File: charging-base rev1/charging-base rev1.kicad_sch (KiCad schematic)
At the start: 11 parts, among them J1 Barrel_Jack, J2 PowerToDino, Q1 NMOS, U1 LM358_DFN

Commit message: added some power questions
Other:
- note added: "What is max current draw of dino? What is current draw of dino when chargning is done? Does current draw change if dino is switched on or switched off? Does the raspi load the source, or is the only load on this circuit the USB battery pack?"
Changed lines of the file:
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@@
+    (effects (font (size 1.27 1.27)) (justify left bottom))
+  )
+  (text "What is max current draw of dino?\nWhat is current draw of dino when chargning is done?\nDoes current draw change if dino is switched on or switched off?\nDoes the raspi load the source, or is the only load on this circuit the USB battery pack?"
+    (at 167.005 127.635 0)
     (effects (font (size 1.27 1.27)) (justify left bottom))
   )

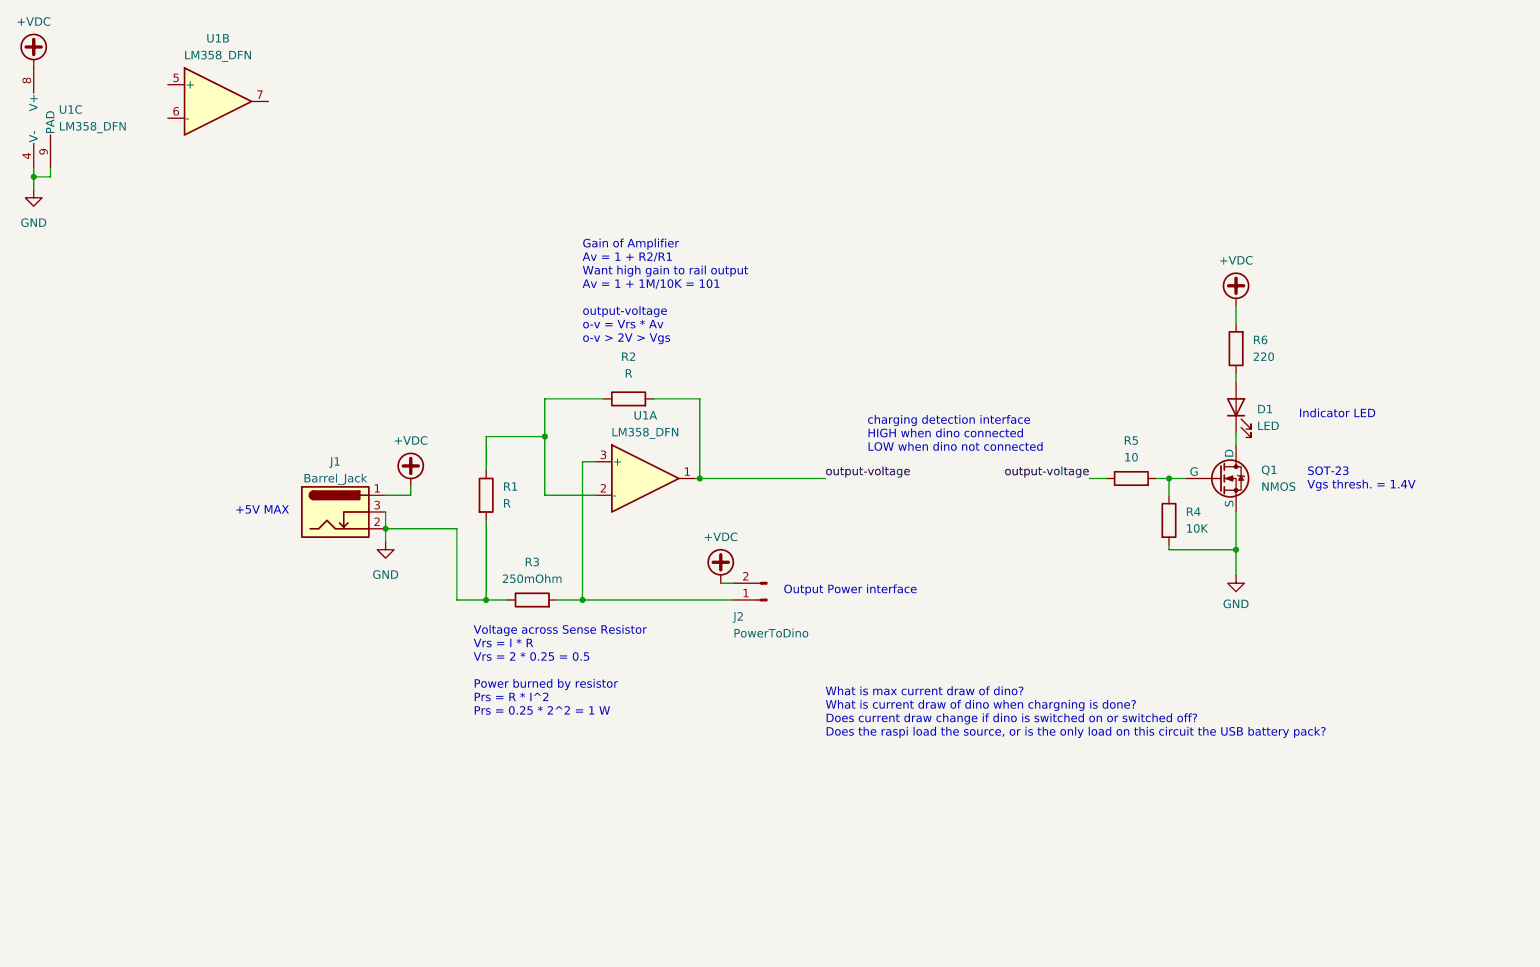
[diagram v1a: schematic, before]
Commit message: finished rev1 of layout, resistor sensor not yet selected
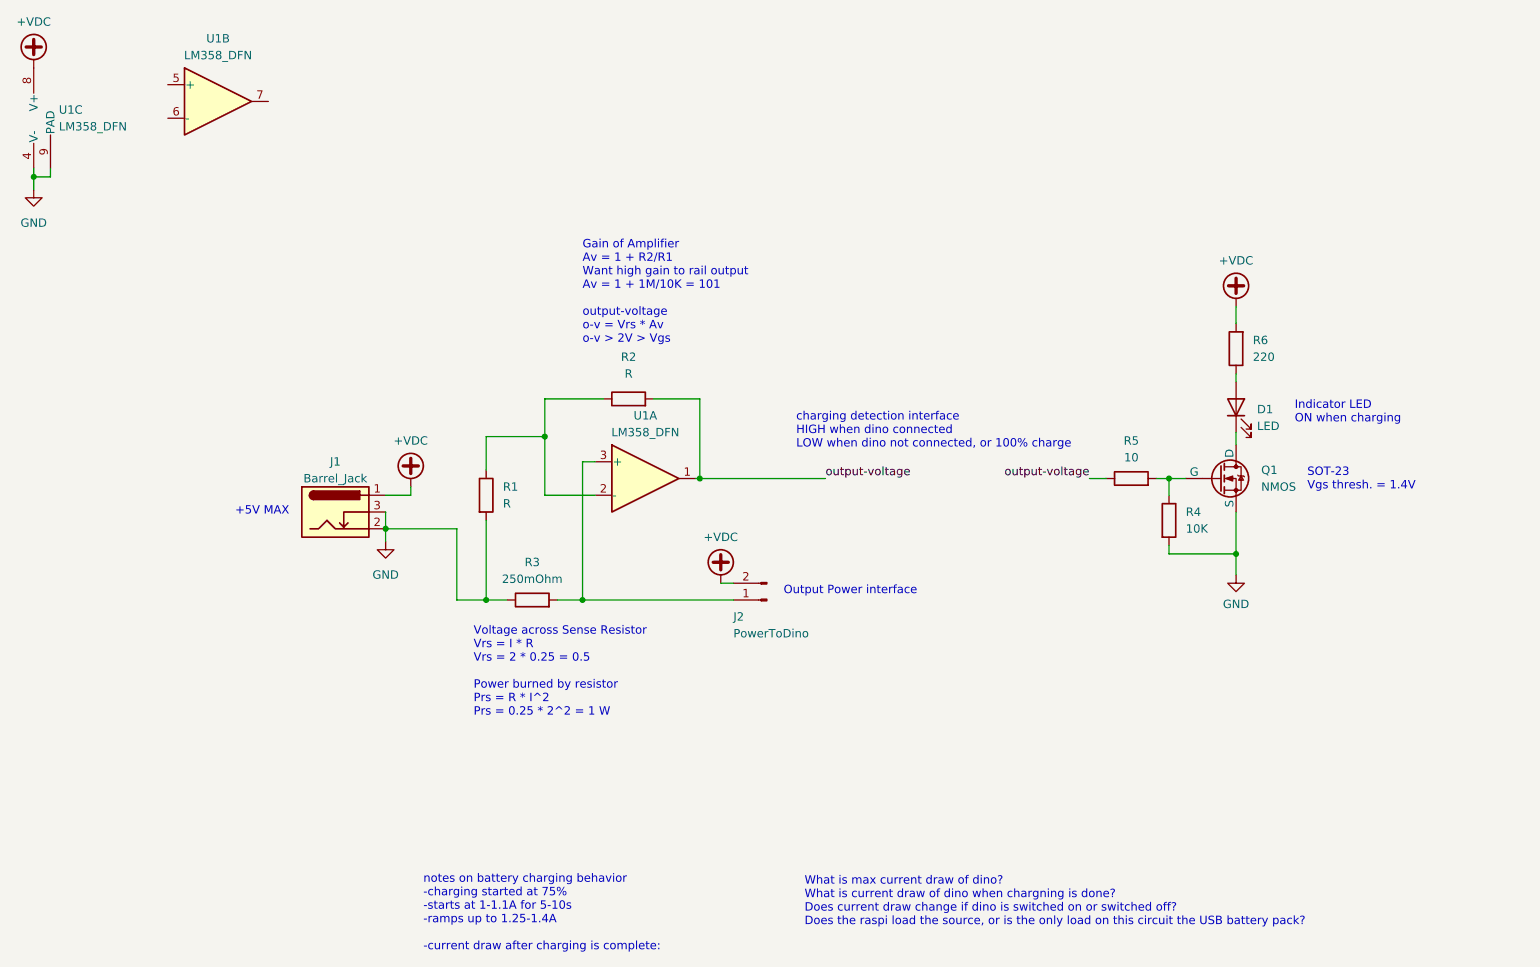
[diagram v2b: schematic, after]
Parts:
- D1: footprint (none) -> LED_THT:LED_D5.0mm
- J2: footprint (none) -> Connector_PinHeader_2.54mm:PinHeader_1x02_P2.54mm_Vertical
- Q1: footprint (none) -> Package_TO_SOT_SMD:SOT-23-3
- R1, R2, R4, R5, R6: footprint (none) -> Capacitor_SMD:C_0603_1608Metric
- R3: footprint (none) -> Resistor_SMD:R_1206_3216Metric
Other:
- note added: "Indicator LED ON when charging"
- note added: "charging detection interface HIGH when dino connected LOW when dino not connected, or 100% charge"
- note added: "notes on battery charging behavior -charging started at 75% -starts at 1-1.1A for 5-10s -ramps up to 1.25-1.4A -current draw after charging is complete:"
- note removed: "Indicator LED"
- note removed: "charging detection interface HIGH when dino connected LOW when dino not connected"
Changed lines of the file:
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@@
   (junction (at 46.99 42.545) (diameter 0) (color 0 0 0 0)
   )
-  (junction (at 229.235 99.06) (diameter 0) (color 0 0 0 0)
+  (junction (at 229.235 99.695) (diameter 0) (color 0 0 0 0)
   )
   (junction (at 130.175 106.68) (diameter 0) (color 0 0 0 0)
@@
     (stroke (width 0) (type default))
   )
+  (wire (pts (xy 229.235 99.695) (xy 229.235 102.87))
+    (stroke (width 0) (type default))
+  )
   (wire (pts (xy 219.075 88.265) (xy 219.075 90.805))
     (stroke (width 0) (type default))
@@
     (stroke (width 0) (type default))
   )
-  (wire (pts (xy 229.235 99.06) (xy 229.235 102.87))
-    (stroke (width 0) (type default))
-  )
   (wire (pts (xy 130.175 85.725) (xy 130.175 106.68))
     (stroke (width 0) (type default))
@@
     (stroke (width 0) (type default))
   )
-  (wire (pts (xy 219.075 99.06) (xy 219.075 98.425))
+  (wire (pts (xy 219.075 99.695) (xy 219.075 98.425))
     (stroke (width 0) (type default))
   )
@@
     (stroke (width 0) (type default))
   )
-  (wire (pts (xy 229.235 93.345) (xy 229.235 99.06))
+  (wire (pts (xy 229.235 93.345) (xy 229.235 99.695))
     (stroke (width 0) (type default))
   )
@@
     (stroke (width 0) (type default))
   )
-  (wire (pts (xy 219.075 99.06) (xy 229.235 99.06))
+  (wire (pts (xy 219.075 99.695) (xy 229.235 99.695))
     (stroke (width 0) (type default))
   )
@@
     (effects (font (size 1.27 1.27)) (justify left bottom))
   )
-  (text "charging detection interface\nHIGH when dino connected\nLOW when dino not connected"
-    (at 173.355 84.455 0)
+  (text "notes on battery charging behavior\n-charging started at 75%\n-starts at 1-1.1A for 5-10s\n-ramps up to 1.25-1.4A\n\n-current draw after charging is complete: \n"
+    (at 106.045 160.02 0)
+    (effects (font (size 1.27 1.27)) (justify left bottom))
+  )
+  (text "charging detection interface\nHIGH when dino connected\nLOW when dino not connected, or 100% charge"
+    (at 162.56 83.82 0)
     (effects (font (size 1.27 1.27)) (justify left bottom))
   )
@@
     (effects (font (size 1.27 1.27)) (justify left bottom))
   )
-  (text "Indicator LED" (at 238.76 79.375 0)
+  (text "Indicator LED\nON when charging" (at 238.125 80.01 0)
     (effects (font (size 1.27 1.27)) (justify left bottom))
   )
   (text "What is max current draw of dino?\nWhat is current draw of dino when chargning is done?\nDoes current draw change if dino is switched on or switched off?\nDoes the raspi load the source, or is the only load on this circuit the USB battery pack?"
-    (at 167.005 127.635 0)
+    (at 163.83 156.21 0)
     (effects (font (size 1.27 1.27)) (justify left bottom))
   )
@@
       (effects (font (size 1.27 1.27)) (justify left))
     )
-    (property "Footprint" "" (at 217.297 94.615 90)
+    (property "Footprint" "Capacitor_SMD:C_0603_1608Metric" (at 217.297 94.615 90)
       (effects (font (size 1.27 1.27)) hide)
     )
@@
       (effects (font (size 1.27 1.27)) (justify right))
     )
-    (property "Footprint" "" (at 231.013 68.58 90)
+    (property "Footprint" "Capacitor_SMD:C_0603_1608Metric" (at 231.013 68.58 90)
       (effects (font (size 1.27 1.27)) hide)
     )
@@
       (effects (font (size 1.27 1.27)))
     )
-    (property "Footprint" "" (at 137.16 77.978 90)
+    (property "Footprint" "Capacitor_SMD:C_0603_1608Metric" (at 137.16 77.978 90)
       (effects (font (size 1.27 1.27)) hide)
     )
@@
       (effects (font (size 1.27 1.27)) (justify left))
     )
-    (property "Footprint" "" (at 113.792 90.805 90)
+    (property "Footprint" "Capacitor_SMD:C_0603_1608Metric" (at 113.792 90.805 90)
       (effects (font (size 1.27 1.27)) hide)
     )
@@
       (effects (font (size 1.27 1.27)) (justify right))
     )
-    (property "Footprint" "" (at 229.235 77.47 0)
+    (property "Footprint" "LED_THT:LED_D5.0mm" (at 229.235 77.47 0)
       (effects (font (size 1.27 1.27)) hide)
     )
@@
       (effects (font (size 1.27 1.27)) (justify left))
     )
-    (property "Footprint" "" (at 231.775 85.725 0)
+    (property "Footprint" "Package_TO_SOT_SMD:SOT-23-3" (at 231.775 85.725 0)
       (effects (font (size 1.27 1.27)) hide)
     )
@@
       (effects (font (size 1.27 1.27)))
     )
-    (property "Footprint" "" (at 213.36 90.043 90)
+    (property "Footprint" "Capacitor_SMD:C_0603_1608Metric" (at 213.36 90.043 90)
       (effects (font (size 1.27 1.27)) hide)
     )
@@
       (effects (font (size 1.27 1.27)))
     )
-    (property "Footprint" "" (at 122.555 108.458 90)
+    (property "Footprint" "Resistor_SMD:R_1206_3216Metric" (at 122.555 108.458 90)
       (effects (font (size 1.27 1.27)) hide)
     )
@@
       (effects (font (size 1.27 1.27)) (justify right))
     )
-    (property "Footprint" "" (at 158.115 106.68 0)
-      (effects (font (size 1.27 1.27)) hide)
-    )
+    (property "Footprint" "Connector_PinHeader_2.54mm:PinHeader_1x02_P2.54mm_Vertical" (at 158.115 106.68 0)
+      (effects (font (size 1.27 1.27)) hide)
+    )

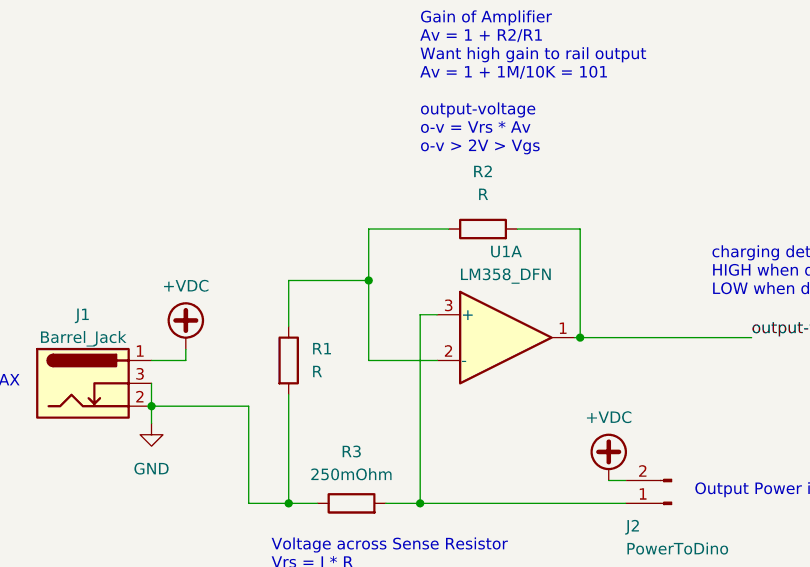
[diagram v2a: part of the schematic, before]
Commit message: added barrel plug source, changed footprint U1
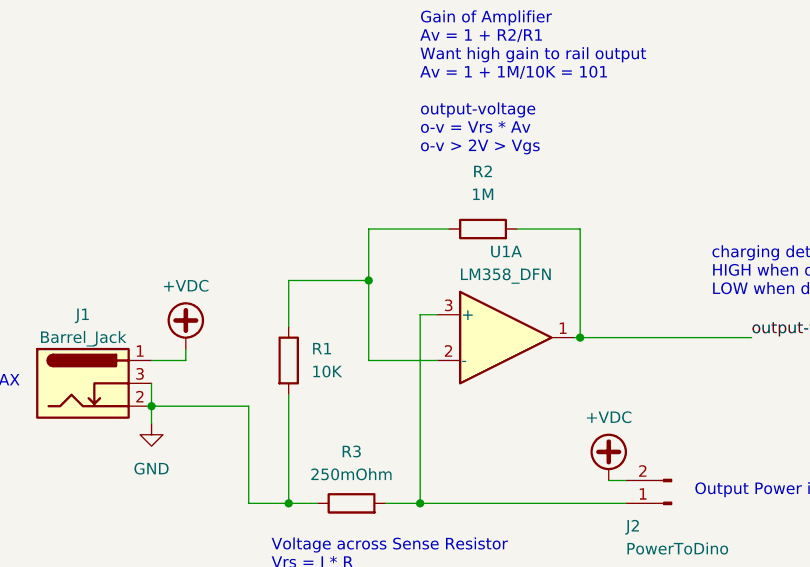
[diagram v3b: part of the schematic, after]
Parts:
- R1: value R -> 10K
- R2: value R -> 1M
- U1: footprint Package_DFN_QFN:DFN-8-1EP_2x2mm_P0.5mm_EP1.05x1.75mm -> LM358DT:SOIC127P600X175-8N
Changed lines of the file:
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@@
       (effects (font (size 1.27 1.27)))
     )
-    (property "Footprint" "Package_DFN_QFN:DFN-8-1EP_2x2mm_P0.5mm_EP1.05x1.75mm" (at 74.93 31.115 0)
+    (property "Footprint" "LM358DT:SOIC127P600X175-8N" (at 74.93 31.115 0)
       (effects (font (size 1.27 1.27)) hide)
     )
@@
       (effects (font (size 1.27 1.27)))
     )
-    (property "Value" "R" (at 137.16 72.39 90)
+    (property "Value" "1M" (at 137.16 72.39 90)
       (effects (font (size 1.27 1.27)))
     )
@@
       (effects (font (size 1.27 1.27)) (justify left))
     )
-    (property "Footprint" "Package_DFN_QFN:DFN-8-1EP_2x2mm_P0.5mm_EP1.05x1.75mm" (at 49.53 33.655 0)
+    (property "Footprint" "LM358DT:SOIC127P600X175-8N" (at 49.53 33.655 0)
       (effects (font (size 1.27 1.27)) hide)
     )
@@
       (effects (font (size 1.27 1.27)) (justify left))
     )
-    (property "Value" "R" (at 118.11 92.075 0)
+    (property "Value" "10K" (at 118.11 92.075 0)
       (effects (font (size 1.27 1.27)) (justify left))
     )
@@
       (effects (font (size 1.27 1.27)))
     )
-    (property "Footprint" "Package_DFN_QFN:DFN-8-1EP_2x2mm_P0.5mm_EP1.05x1.75mm" (at 139.7 88.265 0)
-      (effects (font (size 1.27 1.27)) hide)
-    )
+    (property "Footprint" "LM358DT:SOIC127P600X175-8N" (at 139.7 88.265 0)
+      (effects (font (size 1.27 1.27)) hide)
+    )
